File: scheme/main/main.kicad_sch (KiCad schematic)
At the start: 0 parts

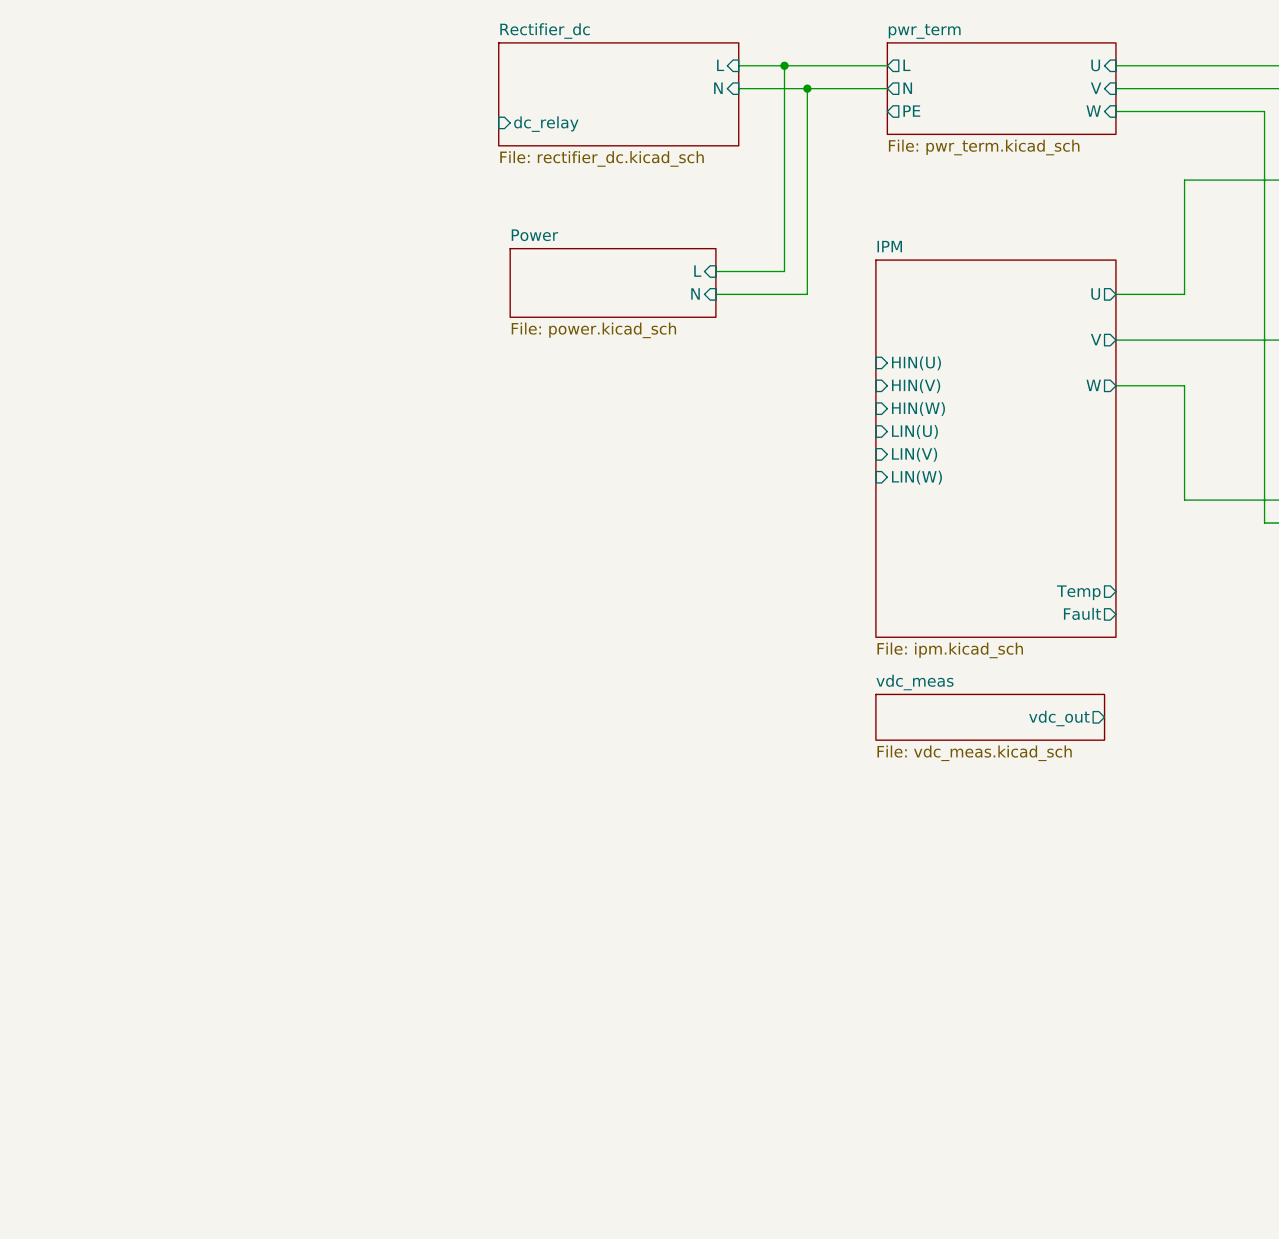
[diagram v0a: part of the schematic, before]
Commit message: digital in & out schematic
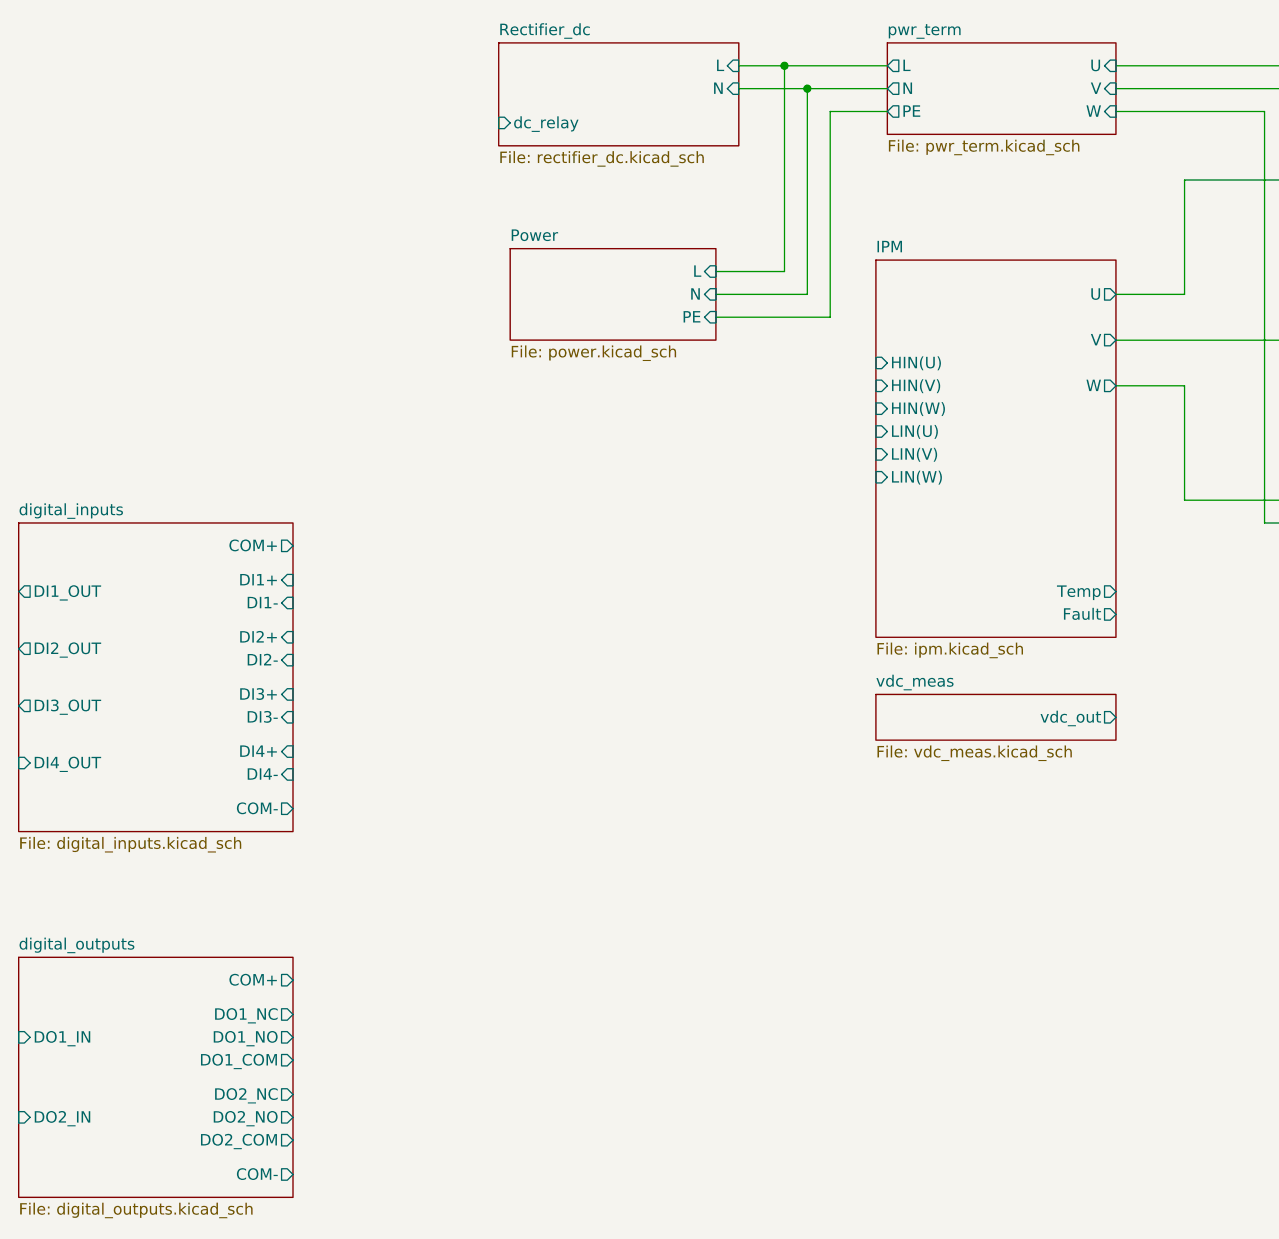
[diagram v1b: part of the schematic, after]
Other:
- added sheet digital_inputs (digital_inputs.kicad_sch)
- added sheet digital_outputs (digital_outputs.kicad_sch)
- sheet Power ports: added PE; removed none

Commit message: di & do terminals
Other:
- added sheet digital_input_term (digital_input_term.kicad_sch)
- added sheet digital_output_term (digital_output_term.kicad_sch)
- sheet digital_inputs ports: added 24V, COM; removed COM+, COM-
- sheet digital_outputs ports: added none; removed COM+, COM-

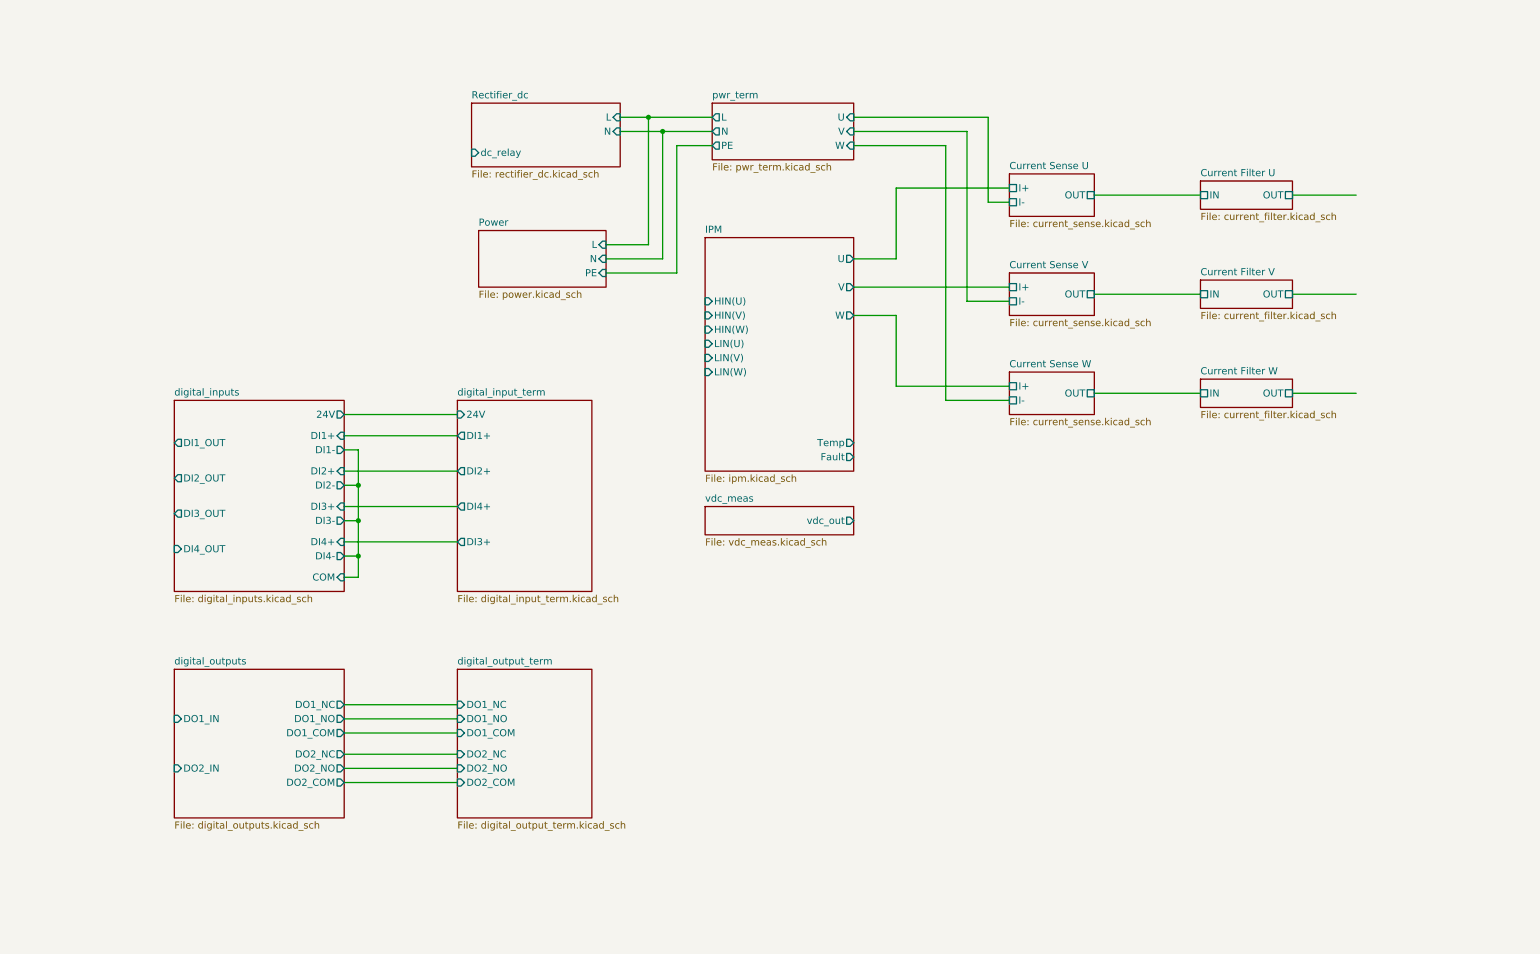
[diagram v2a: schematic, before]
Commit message: toplevel layout, can bus
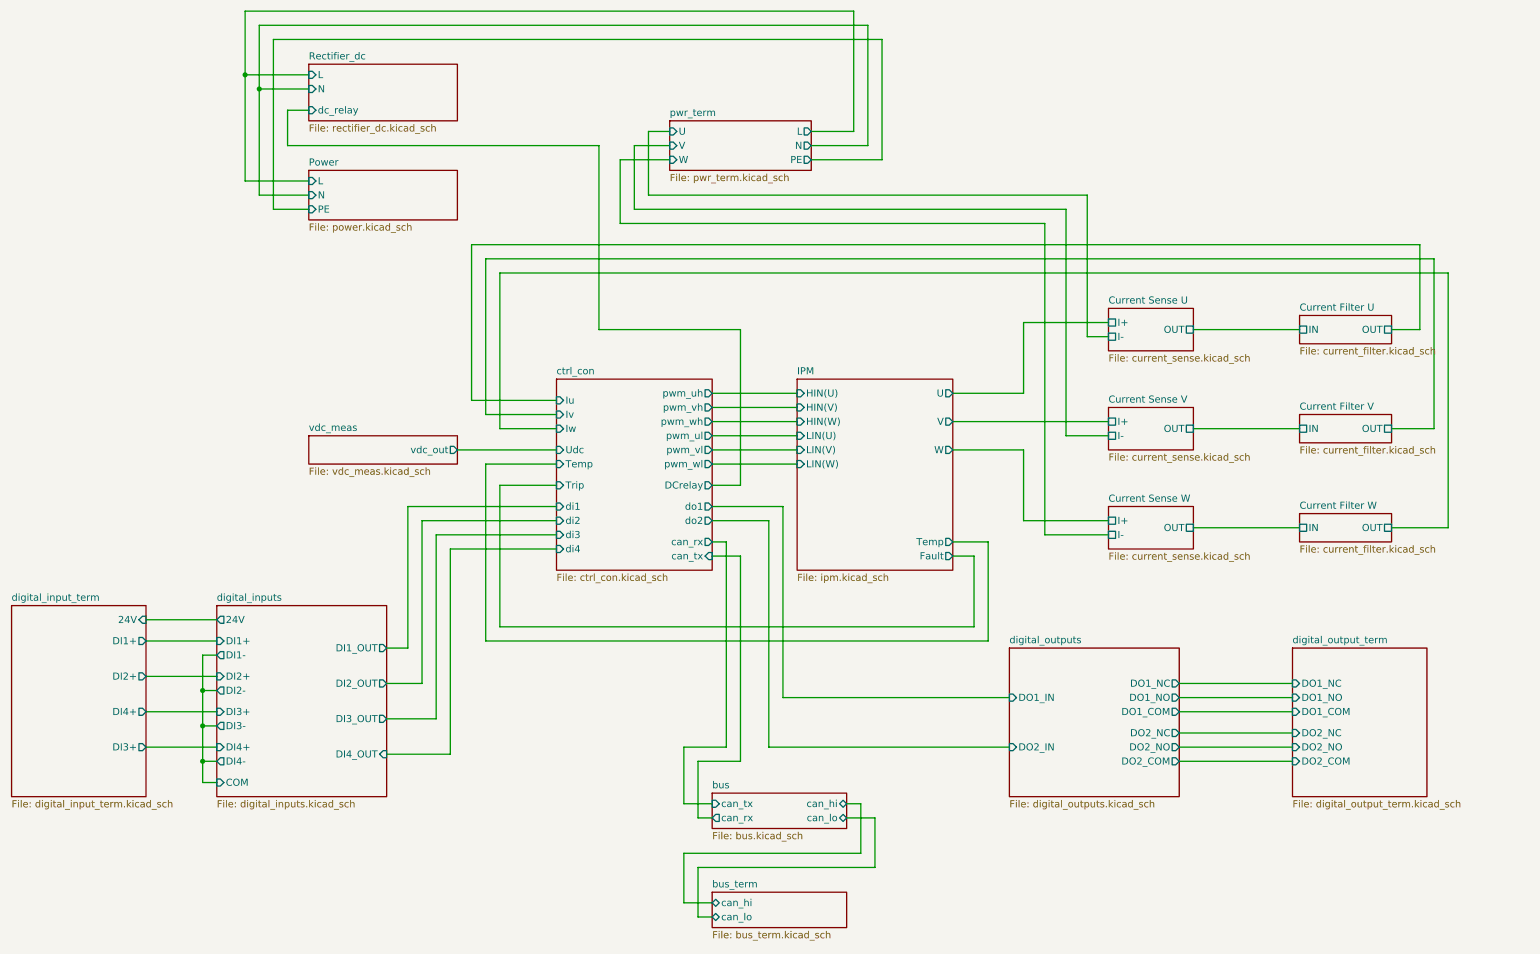
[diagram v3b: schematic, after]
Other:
- added sheet bus (bus.kicad_sch)
- added sheet bus_term (bus_term.kicad_sch)
- added sheet ctrl_con (ctrl_con.kicad_sch)
